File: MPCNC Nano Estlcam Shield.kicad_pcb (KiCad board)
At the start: 2 copper layers, 160 x 100 mm, 96 parts, among them J1 Screw_Terminal_01x02, J10 Conn_01x04_Male, J11 Conn_01x04_Male, J12 Screw_Terminal_01x03, J13 Screw_Terminal_01x03, J14 Screw_Terminal_01x03, J15 Conn_02x03_Odd_Even, J16 Screw_Terminal_01x02, J17 Screw_Terminal_01x02, J18 Screw_Terminal_01x03, J19 Screw_Terminal_01x03, J2 Conn_01x03_Male, J20 Screw_Terminal_01x03, J21 Screw_Terminal_01x03, J22 Screw_Terminal_01x03, J23 Screw_Terminal_01x03, J24 Screw_Terminal_01x03, J25 Screw_Terminal_01x03, J26 Screw_Terminal_01x03, J27 Screw_Terminal_01x03, J28 Conn_01x03_Male, J29 Conn_01x02_Male, J3 Conn_01x06_Male, J4 Screw_Terminal_01x03, J5 Screw_Terminal_01x03, J6 Screw_Terminal_01x03, J7 Conn_01x04_Male, J8 Conn_01x04_Male, J9 Conn_01x04_Male, U1 LM358, U2 LTV-847, U3 LTV-847, U4 LTV-847, U5 ULN2003, U6 L7805, U7 ATtiny45-20PU

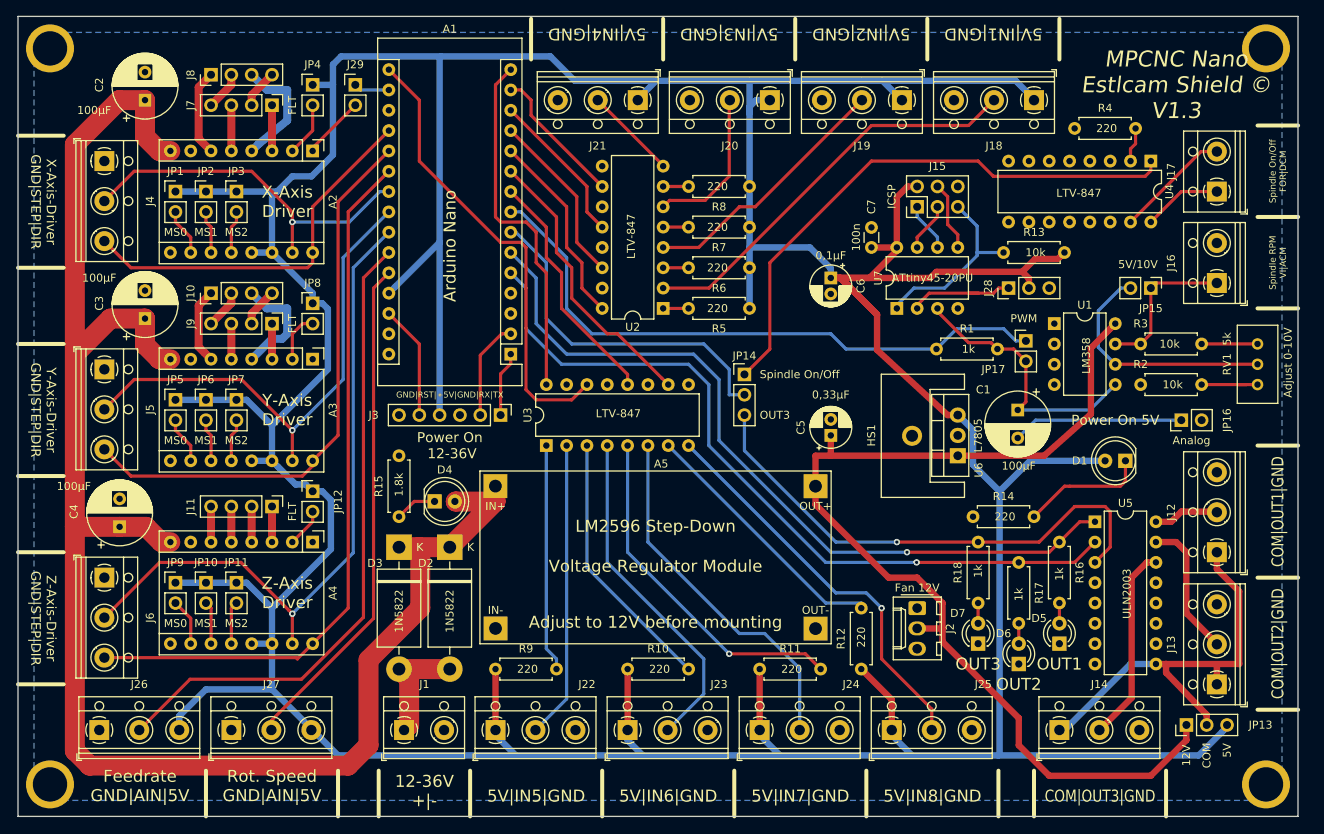
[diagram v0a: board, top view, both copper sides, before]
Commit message: V1.4
- Version 1.4 of MPCNC Nano Estlcam Shield
   PCB schematic changes:
    # Changed LED colours (D1:red, D4:green, D5-7:Clear/red)
   PCB layout changes:
    + Footprints for LEDs added to project footprint library ("MPCNC_Shield_Footprints").
    # Changed footprint of LEDs
    # Moved silk screen reference fo L7805 (U6). Reference was hidden by heatsink
    + Added LED 3D models to footprint. LEDs show correct color for 3D model (green, red, white[clear])
    # Changed 3D model for potentiometer (KiCAD standard library model now available in latest KiCAD release 5.10)
    # Changed 3D model for screw terminal blocks (J1; J4-6; J12-14; J16-J17; J18-27)
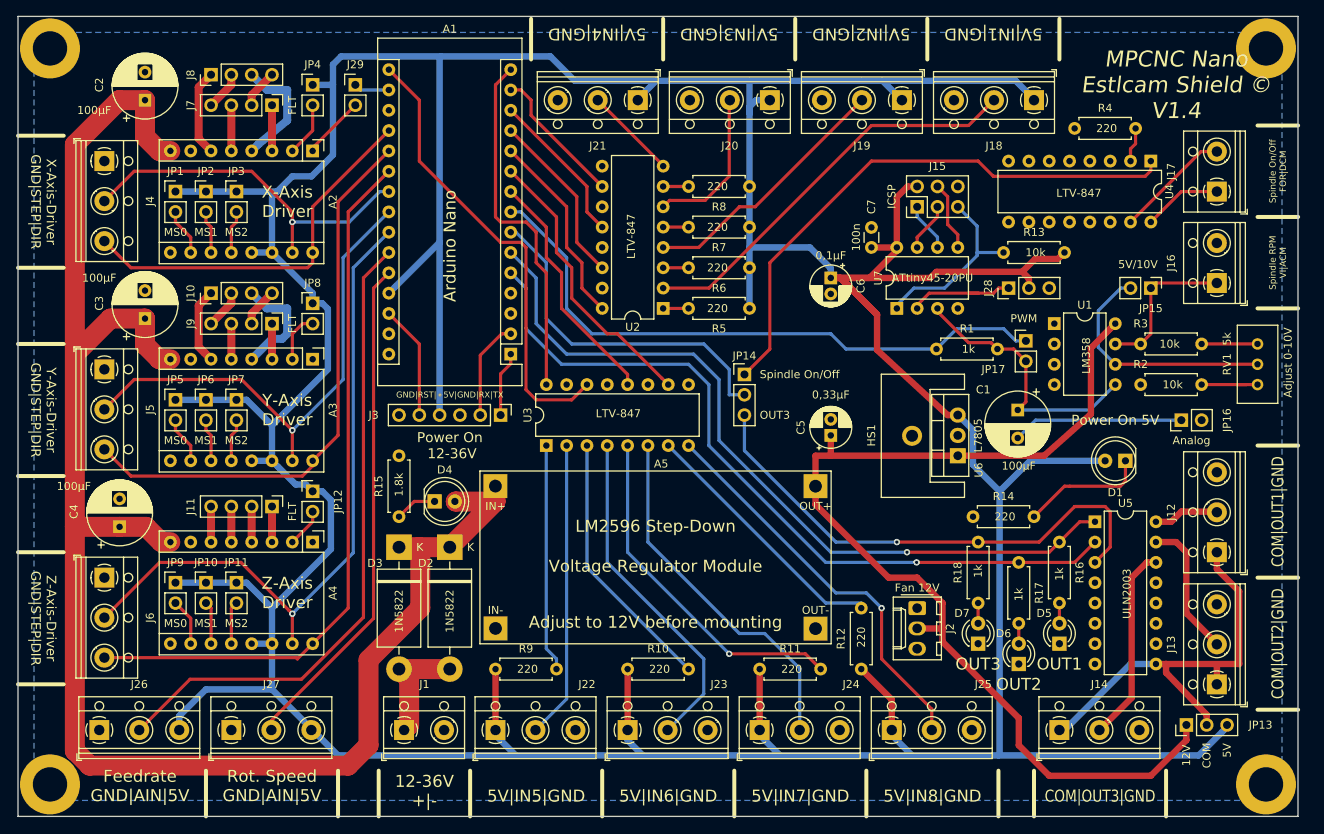
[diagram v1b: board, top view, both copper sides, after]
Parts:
- D1: value LED GREEN -> LED RED; footprint LED_THT:LED_D5.0mm -> MPCNC_Shield_Footprints:LED_D5.0mm_Red
- D4: value LED RED -> LED GREEN; footprint LED_THT:LED_D5.0mm -> MPCNC_Shield_Footprints:LED_D5.0mm_Green
- D5, D6, D7: value LED RED -> LED CLEAR/RED; footprint LED_THT:LED_D3.0mm -> MPCNC_Shield_Footprints:LED_D3.0mm_Clear
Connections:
- A1 pad 18: Net-(A1-Pad18) -> (no net)
- A1 pad 3: Net-(A1-Pad3) -> (no net)
- A1 pad 30: Net-(A1-Pad30) -> (no net)
- J2 pad 3: Net-(J2-Pad3) -> (no net)
- U5 pad 10: Net-(U5-Pad10) -> (no net)
- U5 pad 11: Net-(U5-Pad11) -> (no net)
- U5 pad 12: Net-(U5-Pad12) -> (no net)
- U5 pad 13: Net-(U5-Pad13) -> (no net)
- U5 pad 4: Net-(U5-Pad4) -> (no net)
- U5 pad 5: Net-(U5-Pad5) -> (no net)
- U5 pad 6: Net-(U5-Pad6) -> (no net)
- U5 pad 7: Net-(U5-Pad7) -> (no net)
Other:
- board text added: "MPCNC Nano Estlcam Shield © V1.4"
- board text removed: "MPCNC Nano Estlcam Shield © V1.3"
